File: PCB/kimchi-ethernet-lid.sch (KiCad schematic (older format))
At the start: 58 parts, among them J1 DF40HC(3.5)-60DS, J2 DF40HC(3.5)-60DS, J3 ARJM11C7-502-AB-ER2-T, U1 24C32, U2 TLV75712PDBVR, U3 KSZ9031RNXCC, Y1 ABM3-25.000MHZ-D2Y-T

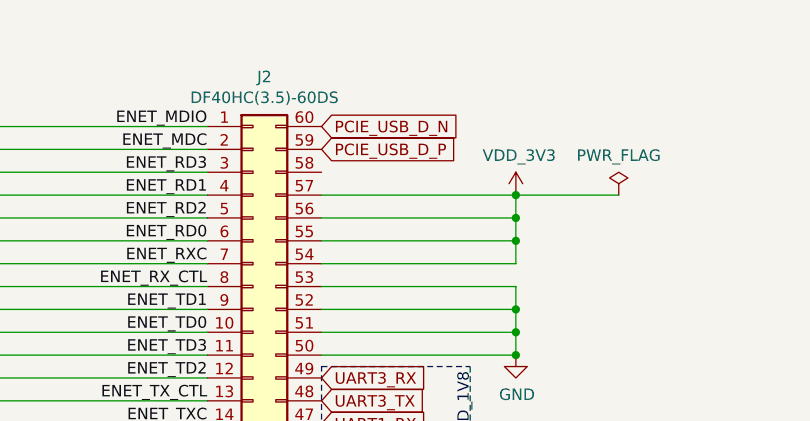
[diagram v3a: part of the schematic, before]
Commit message: Memory Module
Memory module moved, USB to PCIe passthrough added. BOM created in libreoffice format, CSV from component fields also generated.
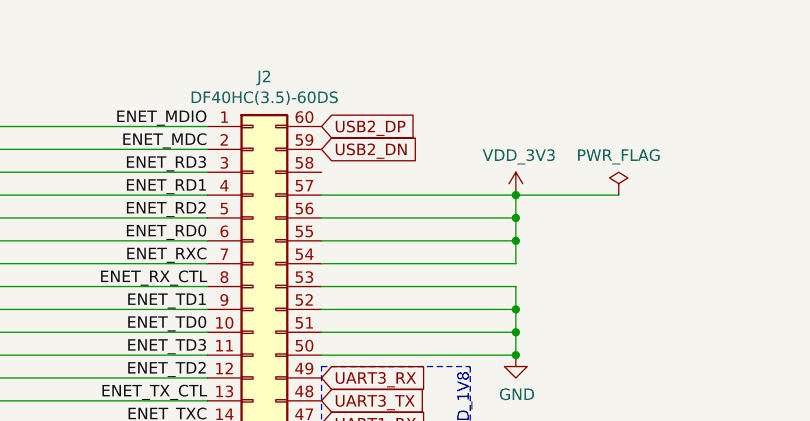
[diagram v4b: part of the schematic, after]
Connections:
- net labels removed: PCIE_USB_D_N, PCIE_USB_D_P
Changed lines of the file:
@@
 Wire Wire Line
 	10800 2750 10800 2850
-Text GLabel 9950 1250 2    50   Input ~ 0
-PCIE_USB_D_N
-Text GLabel 9950 1350 2    50   Input ~ 0
-PCIE_USB_D_P
 Text GLabel 9950 2450 2    50   Input ~ 0
 UART3_TX
@@
 Wire Wire Line
 	5000 9950 5200 9950
+Text GLabel 9950 1250 2    50   Input ~ 0
+USB2_DP
+Text GLabel 9950 1350 2    50   Input ~ 0
+USB2_DN
 $EndSCHEMATC

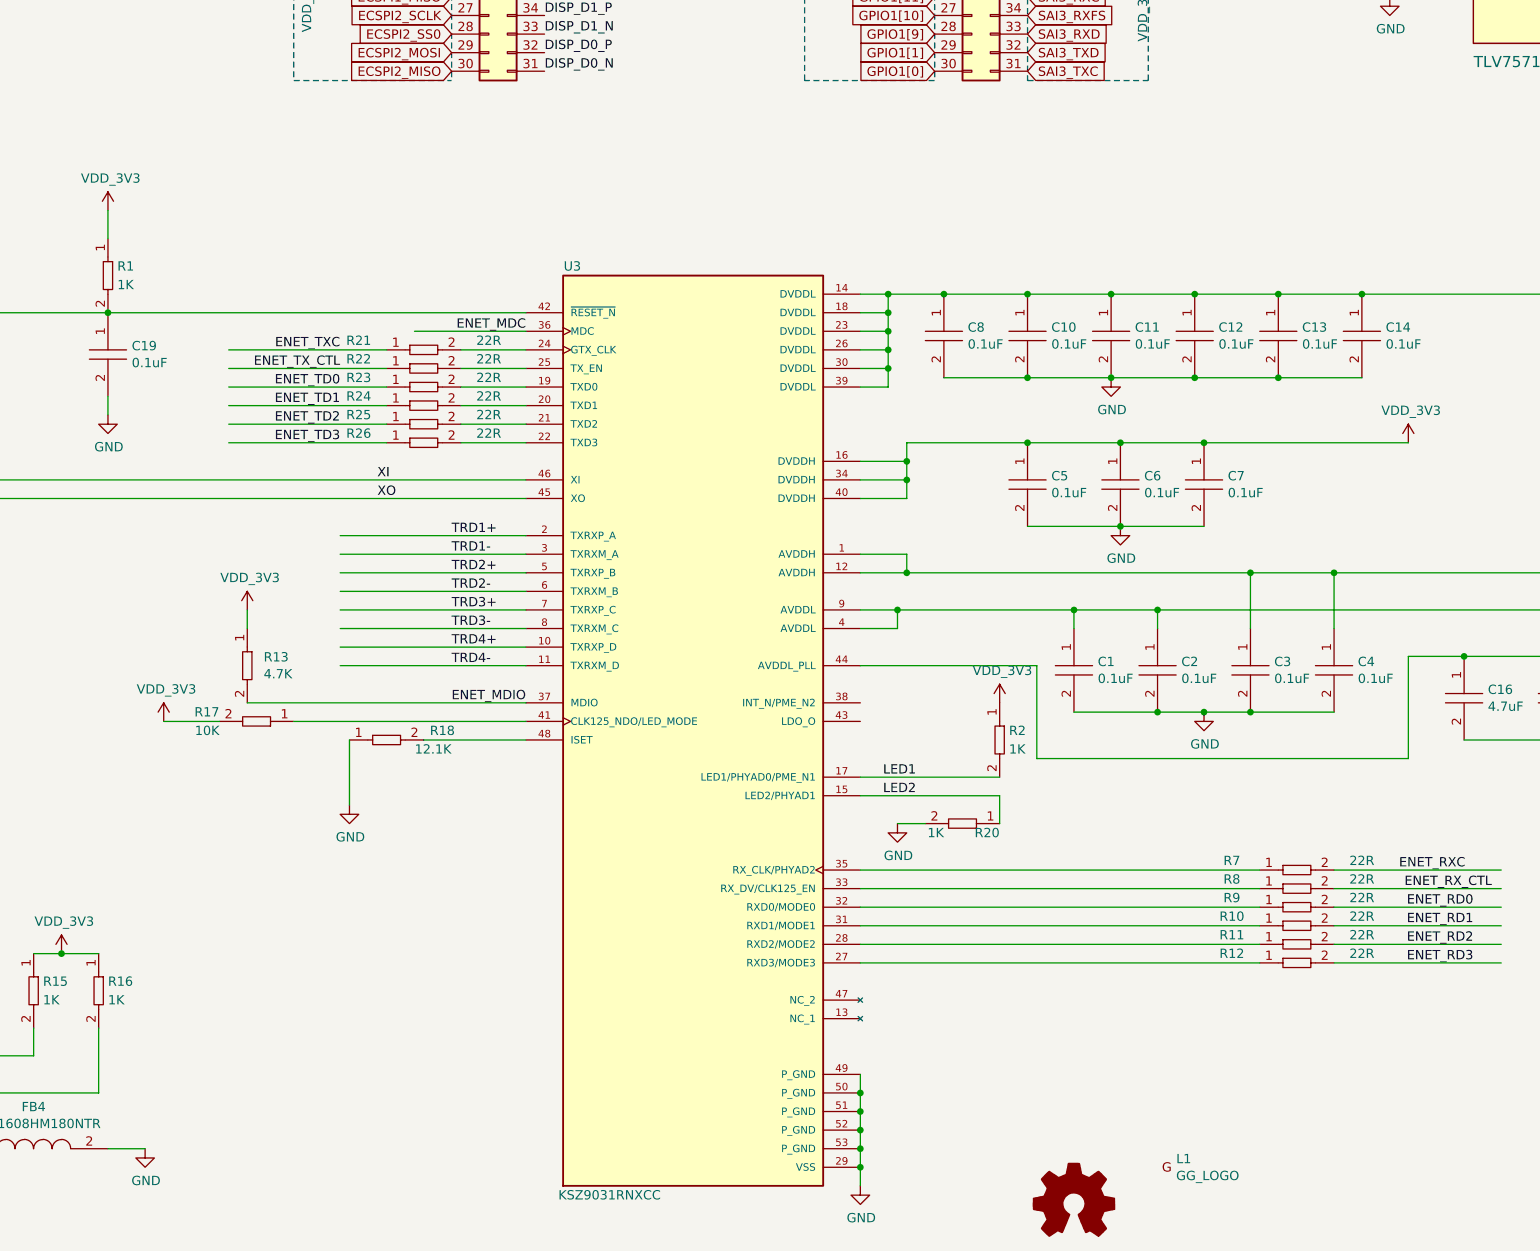
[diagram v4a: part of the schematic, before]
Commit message: Pullups
Pullup resistors added to RGMII interface setup on boot.
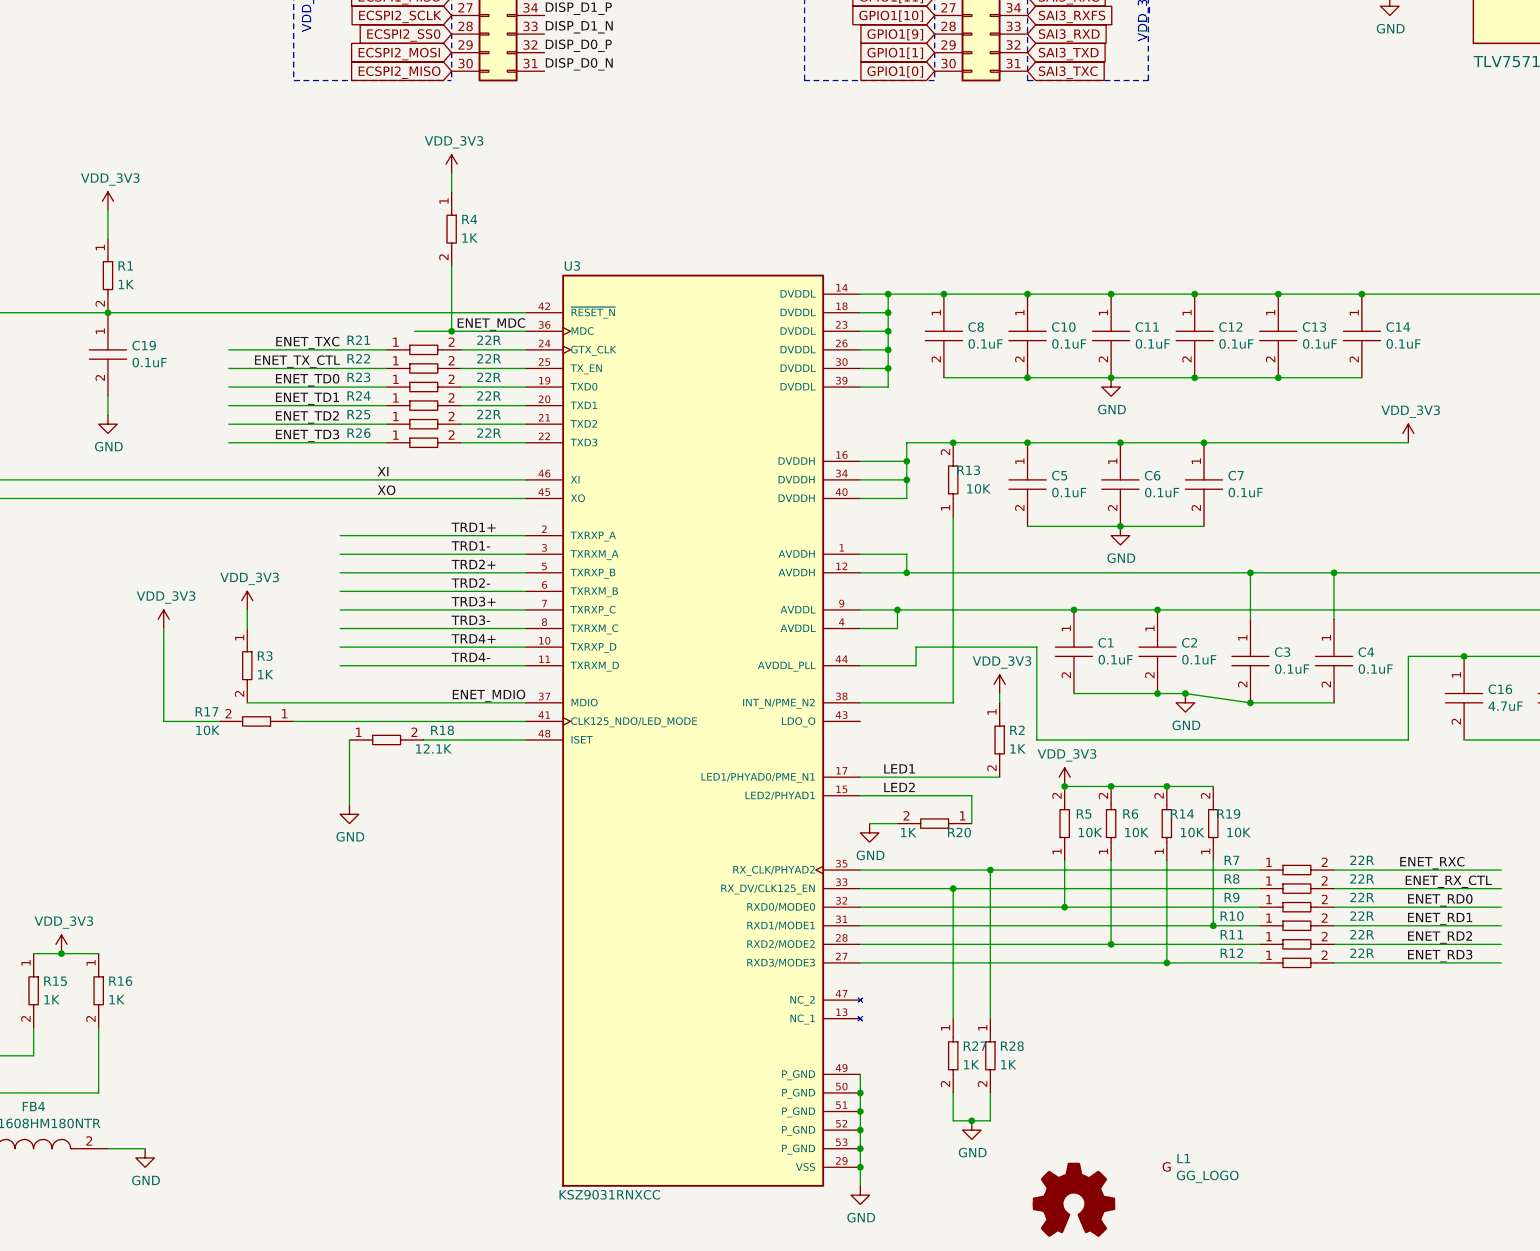
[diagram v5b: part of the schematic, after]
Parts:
- removed R13: RC0402FR-074K7L, kimchi_ulid:R0402, symbol kimchi_ulid:RC0402FR-074K7L
- added R13, R14, R19, R5, R6: RC0402FR-0710KL, kimchi_ulid:R0402, symbol kimchi_ulid:RC0402FR-0710KL
- added R27, R28, R3, R4: RC0402FR-071KL, kimchi_ulid:R0402, symbol kimchi_ulid:RC0402FR-071KL
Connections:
- wire segments 226 -> 253
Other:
- moved on the sheet: C1, C2, C3, C4, R20

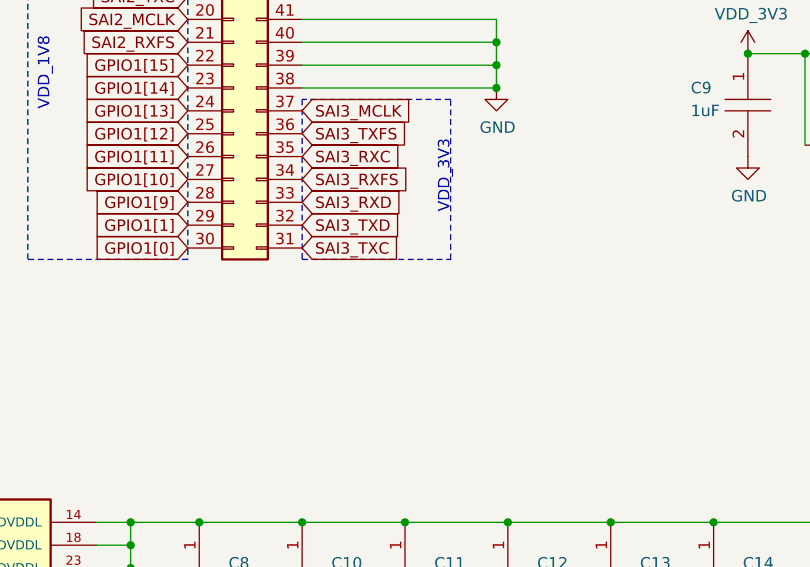
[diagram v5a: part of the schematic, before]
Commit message: DRC and Sys_Reset
Fixed some small DRC violations. zeroed out soldermask settings so that fab can decide their own. Tied SYS_RESET signal to muxable GPIO pin on Kimchi header.
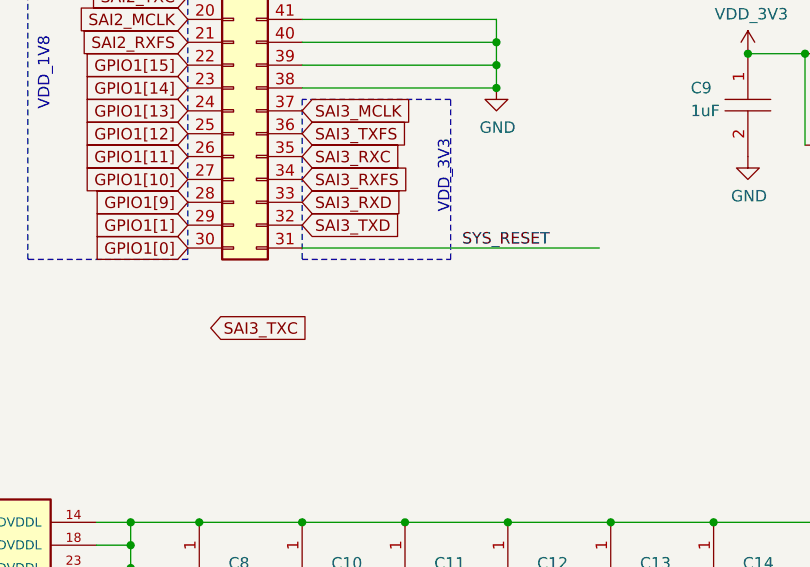
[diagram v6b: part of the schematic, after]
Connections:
- wire segments 253 -> 254
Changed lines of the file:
@@
 Text GLabel 9950 4050 2    50   Input ~ 0
 SAI3_TXD
-Text GLabel 9950 4150 2    50   Input ~ 0
+Text GLabel 9550 4500 2    50   Input ~ 0
 SAI3_TXC
 Text GLabel 9950 3650 2    50   Input ~ 0
@@
 Wire Wire Line
 	9800 7550 9800 7500
+Wire Wire Line
+	11250 4150 9950 4150
+Text Label 10650 4150 0    50   ~ 0
+SYS_RESET
 $EndSCHEMATC
